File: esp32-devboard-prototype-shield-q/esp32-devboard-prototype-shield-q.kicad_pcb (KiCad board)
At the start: 2 copper layers, 40.6 x 20.3 mm, 3 parts, among them J1 11x10, J1 Conn_01x12, J2 Conn_01x12

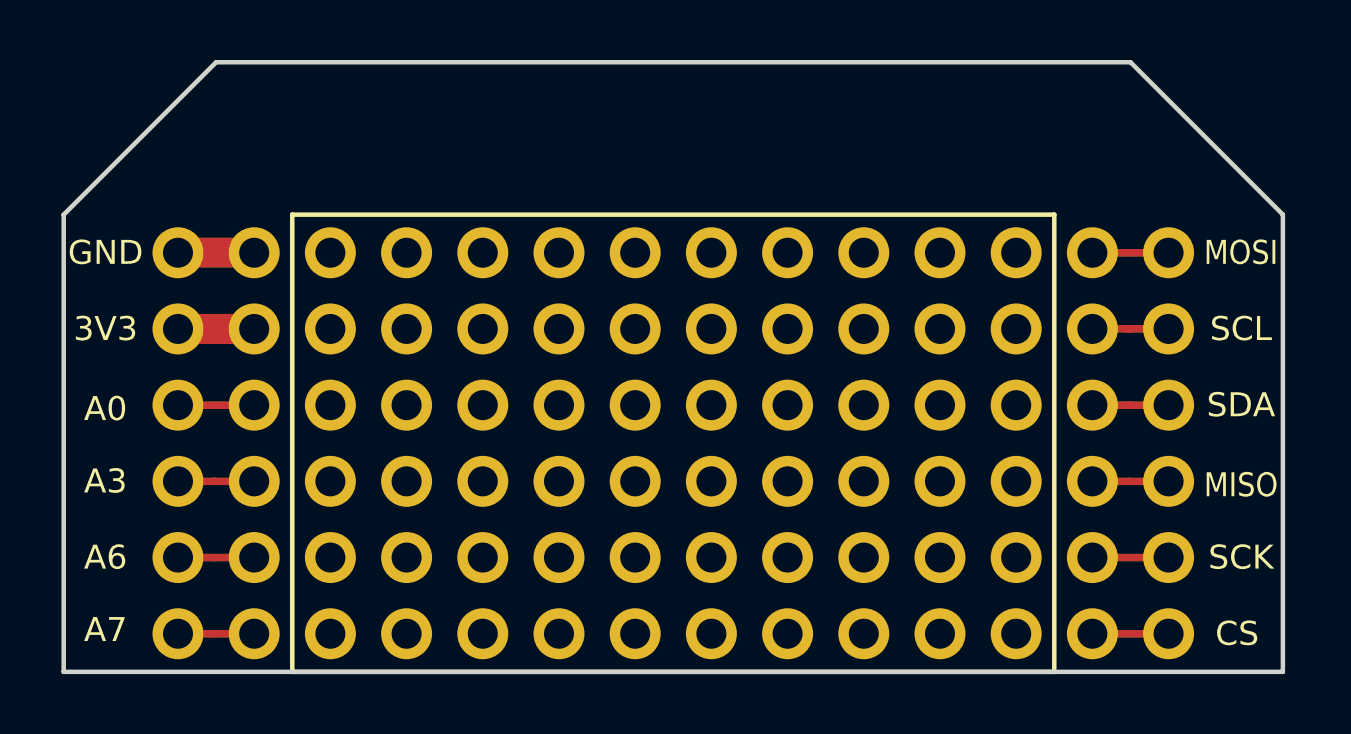
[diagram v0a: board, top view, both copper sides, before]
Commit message: follow pinout changes
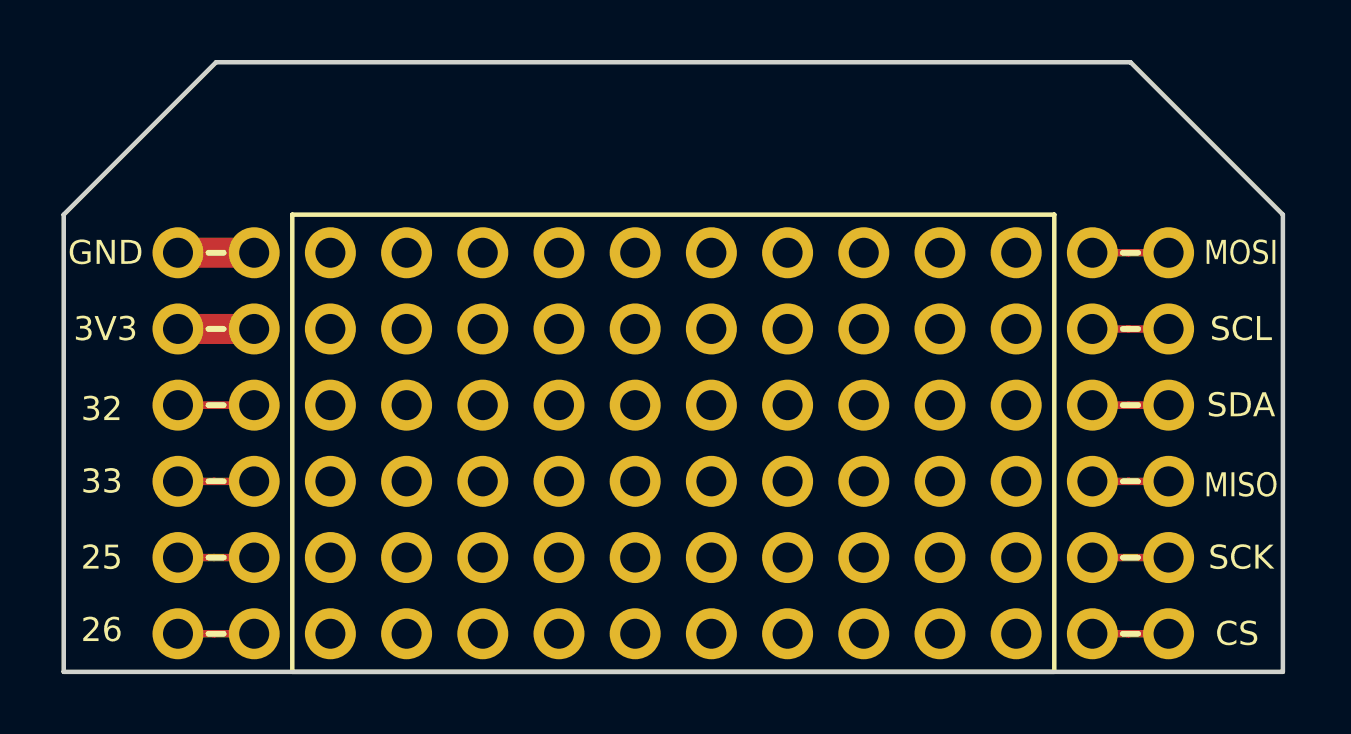
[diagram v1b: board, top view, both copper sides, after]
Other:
- board text added: "25"
- board text added: "26"
- board text added: "32"
- board text added: "33"
- board text added: "A14"
- board text added: "A15"
- board text added: "DAC1"
- board text added: "DAC2"
- board text removed: "34"
- board text removed: "35"
- board text removed: "36"
- board text removed: "39"
- board text removed: "A0"
- board text removed: "A3"
- board text removed: "A6"
- board text removed: "A7"
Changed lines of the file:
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@@
   (general
     (thickness 1.6)
-    (drawings 33)
+    (drawings 45)
     (tracks 20)
     (zones 0)
@@
     )
   )
+  (gr_line (start 166.116 96.52) (end 166.624 96.52) (layer F.SilkS) (width 0.2))
+  (gr_line (start 166.116 93.98) (end 166.624 93.98) (layer F.SilkS) (width 0.2))
+  (gr_line (start 166.116 91.44) (end 166.624 91.44) (layer F.SilkS) (width 0.2))
+  (gr_line (start 166.116 88.9) (end 166.624 88.9) (layer F.SilkS) (width 0.2))
+  (gr_line (start 166.116 86.36) (end 166.624 86.36) (layer F.SilkS) (width 0.2))
+  (gr_line (start 166.116 83.82) (end 166.624 83.82) (layer F.SilkS) (width 0.2))
+  (gr_line (start 135.636 96.52) (end 136.144 96.52) (layer F.SilkS) (width 0.2))
+  (gr_line (start 135.636 93.98) (end 136.144 93.98) (layer F.SilkS) (width 0.2))
+  (gr_line (start 135.636 91.44) (end 136.144 91.44) (layer F.SilkS) (width 0.2))
+  (gr_line (start 135.636 88.9) (end 136.144 88.9) (layer F.SilkS) (width 0.2))
+  (gr_line (start 135.636 86.36) (end 136.144 86.36) (layer F.SilkS) (width 0.2))
+  (gr_line (start 135.636 83.82) (end 136.144 83.82) (layer F.SilkS) (width 0.2))
   (gr_text "ESP32 DEV BOARD\nQUARTER SHIELD" (at 151.384 80.01) (layer B.SilkS)
     (effects (font (size 1.5 1.5) (thickness 0.3)) (justify mirror))
@@
     (effects (font (size 0.8 0.7) (thickness 0.15)))
   )
-  (gr_text 35 (at 132.08 96.393) (layer B.SilkS)
-    (effects (font (size 0.8 0.8) (thickness 0.15)) (justify mirror))
-  )
-  (gr_text A7 (at 132.207 96.393) (layer F.SilkS)
-    (effects (font (size 0.8 0.8) (thickness 0.15)))
-  )
-  (gr_text 34 (at 132.08 93.98) (layer B.SilkS)
-    (effects (font (size 0.8 0.8) (thickness 0.15)) (justify mirror))
-  )
-  (gr_text A6 (at 132.207 93.98) (layer F.SilkS)
-    (effects (font (size 0.8 0.8) (thickness 0.15)))
-  )
-  (gr_text 39 (at 132.08 91.44) (layer B.SilkS)
-    (effects (font (size 0.8 0.8) (thickness 0.15)) (justify mirror))
-  )
-  (gr_text A3 (at 132.207 91.44) (layer F.SilkS)
-    (effects (font (size 0.8 0.8) (thickness 0.15)))
-  )
-  (gr_text "A0\n" (at 132.207 89.027) (layer F.SilkS)
-    (effects (font (size 0.8 0.8) (thickness 0.15)))
-  )
-  (gr_text 36 (at 132.08 89.027) (layer B.SilkS)
-    (effects (font (size 0.8 0.8) (thickness 0.15)) (justify mirror))
+  (gr_text 26 (at 132.08 96.393) (layer F.SilkS)
+    (effects (font (size 0.8 0.8) (thickness 0.15)))
+  )
+  (gr_text DAC2 (at 132.08 96.393) (layer B.SilkS)
+    (effects (font (size 0.8 0.7) (thickness 0.15)) (justify mirror))
+  )
+  (gr_text 25 (at 132.08 93.98) (layer F.SilkS)
+    (effects (font (size 0.8 0.8) (thickness 0.15)))
+  )
+  (gr_text DAC1 (at 132.08 93.98) (layer B.SilkS)
+    (effects (font (size 0.8 0.7) (thickness 0.15)) (justify mirror))
+  )
+  (gr_text 33 (at 132.08 91.44) (layer F.SilkS)
+    (effects (font (size 0.8 0.8) (thickness 0.15)))
+  )
+  (gr_text A15 (at 132.08 91.44) (layer B.SilkS)
+    (effects (font (size 0.8 0.8) (thickness 0.15)) (justify mirror))
+  )
+  (gr_text A14 (at 132.08 89.027) (layer B.SilkS)
+    (effects (font (size 0.8 0.8) (thickness 0.15)) (justify mirror))
+  )
+  (gr_text 32 (at 132.08 89.027) (layer F.SilkS)
+    (effects (font (size 0.8 0.8) (thickness 0.15)))
   )
   (gr_text 3V3 (at 132.08 86.36) (layer B.SilkS)
